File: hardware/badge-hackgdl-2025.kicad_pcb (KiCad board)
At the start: 2 copper layers, 73.4 x 79.5 mm, 53 parts, among them J1 ADDON, J2 Battery, P1 USB_C_Plug_USB2.0, Q1 DMG3415U-7, Q2 MMBT2222A, SW1 ON, SW2 RESET, SW3 BOOT, SW4 LEFT, SW5 BACK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

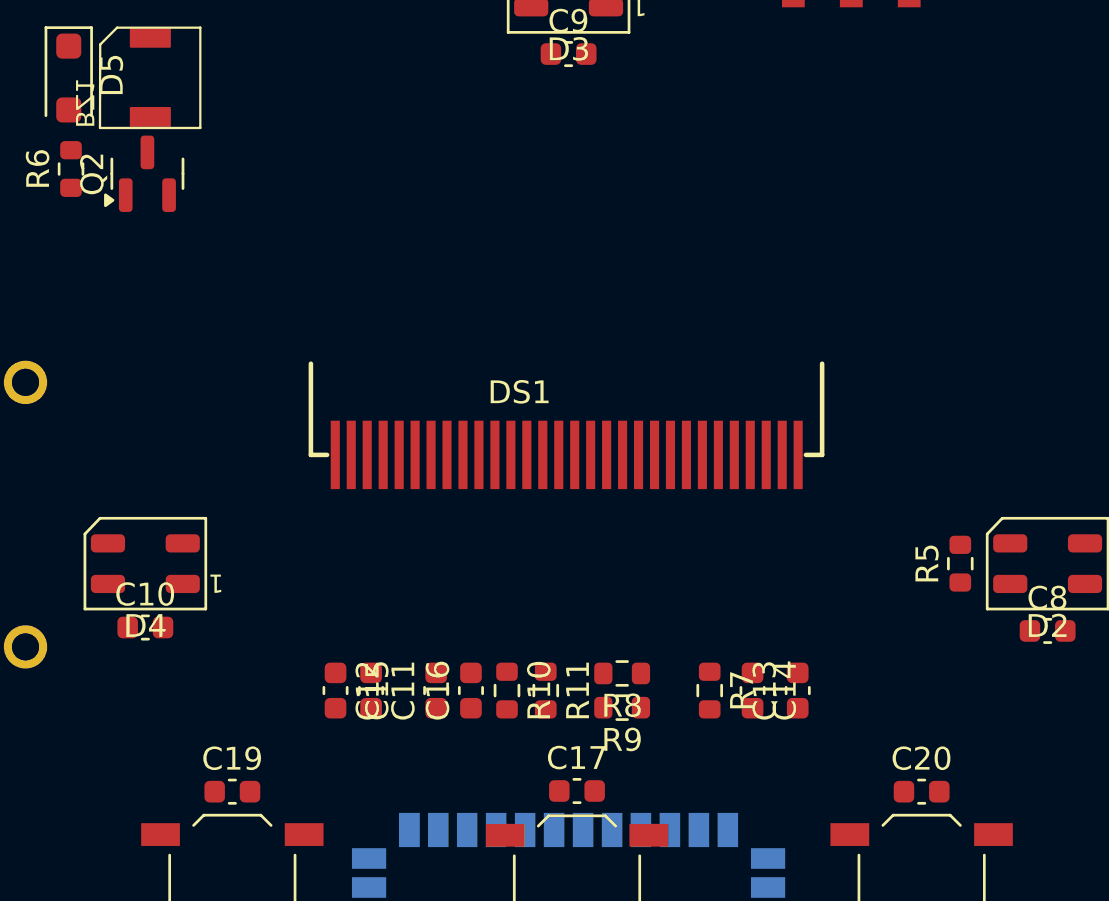
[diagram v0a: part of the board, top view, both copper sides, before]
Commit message: feat(hw): change oled footprint
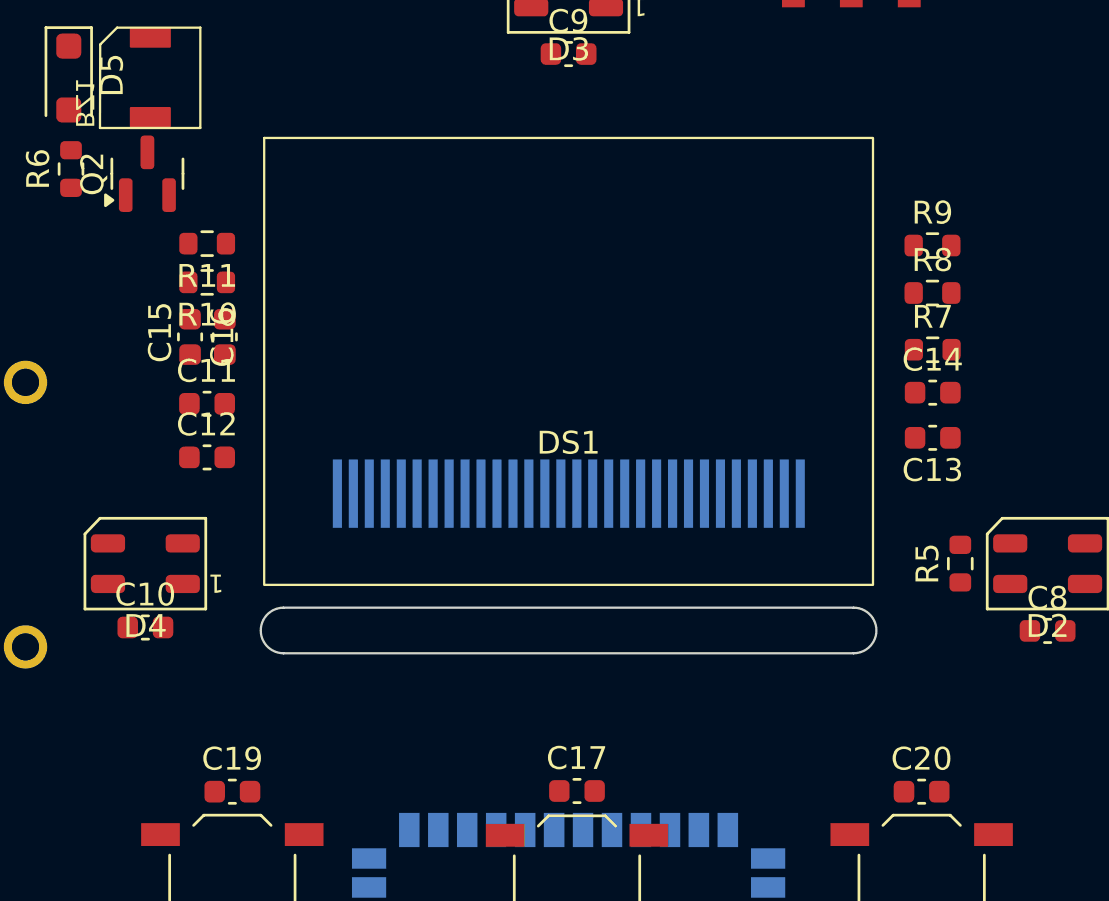
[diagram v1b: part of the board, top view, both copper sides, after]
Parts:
- DS1: footprint Footprints:ssd1306_oled_conn -> Footprints:ssd1306_oled_conn_through_the_oled
- R4: value 10K -> 10k
- moved R11 24.6 mm to (117.8, 47.7), turned to 180 degrees
- moved R9 24.4 mm to (149.6, 47.8), turned to 0 degrees
- moved R10 22.2 mm to (117.8, 49.4), turned to 180 degrees
- moved R8 21.5 mm to (149.6, 49.9), turned to 0 degrees
- moved C16 19.8 mm to (117.1, 51.8), turned to -90 degrees
- moved C15 18.1 mm to (118.6, 51.8), turned to -90 degrees
- moved R7 17.9 mm to (149.6, 52.3), turned to 0 degrees
- moved C14 15.3 mm to (149.6, 54.2), turned to 0 degrees
- moved C11 14.5 mm to (117.8, 54.7), turned to 0 degrees
- moved C13 12.6 mm to (149.6, 56.2), turned to 180 degrees
- moved C12 11.7 mm to (117.8, 57.1), turned to 0 degrees
- moved DS1 3.11 mm to (133.7, 56.9)
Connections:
- J1 pad 5: unconnected-(J1-Pin_5-Pad5) -> /GPIO1
- J1 pad 6: unconnected-(J1-Pin_6-Pad6) -> /GPIO2
- U2 pad 6: unconnected-(U2-IO6-Pad6) -> /GPIO1
- U2 pad 7: unconnected-(U2-IO7-Pad7) -> /GPIO2
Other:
- copper layers 2 -> 11

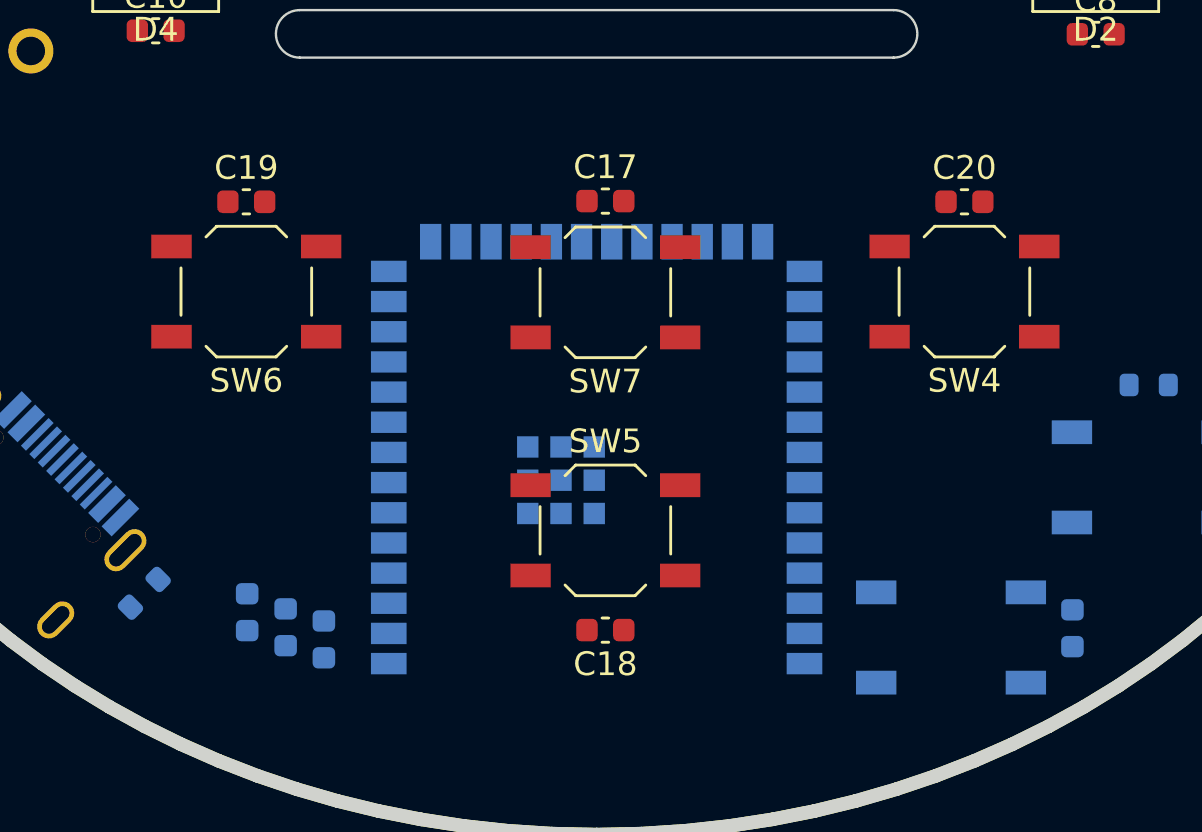
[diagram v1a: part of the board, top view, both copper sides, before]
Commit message: feat(hw): move buttons
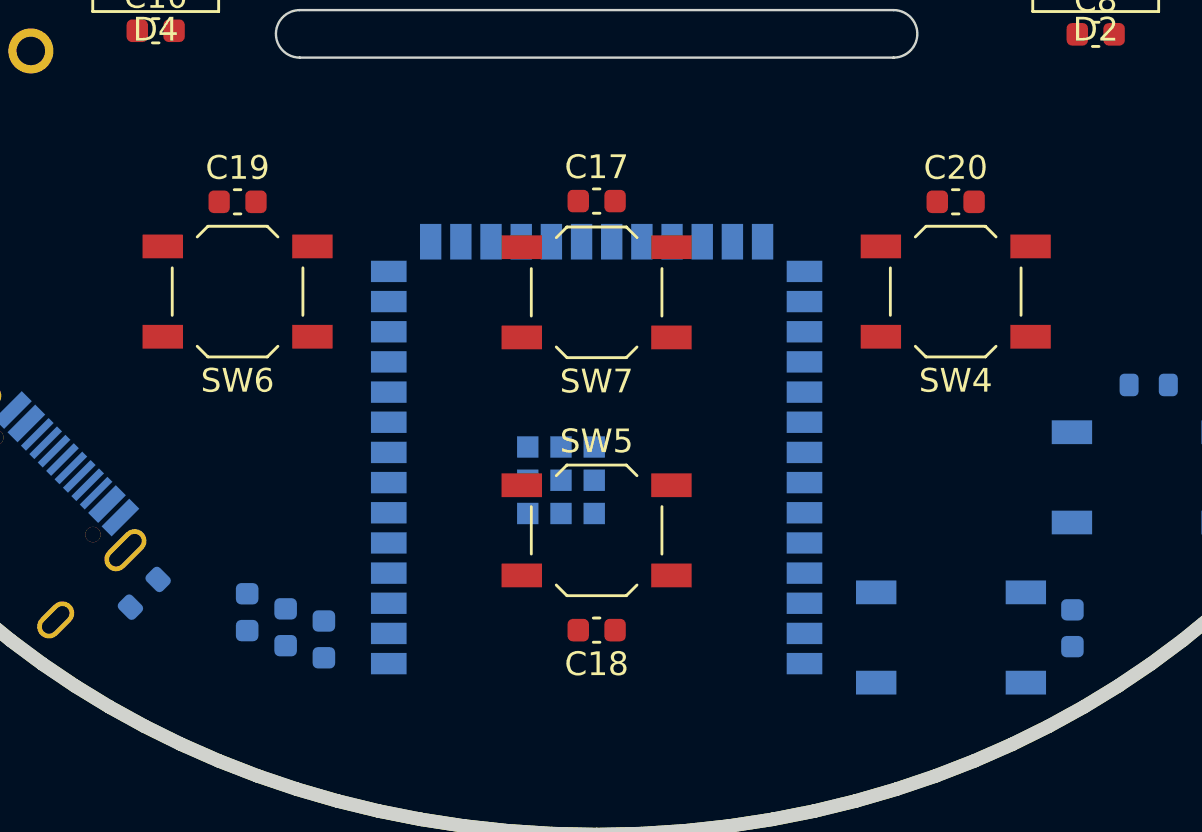
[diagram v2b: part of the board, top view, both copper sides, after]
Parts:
- moved C17 0.37 mm to (133.7, 71.7)
- moved C18 0.37 mm to (133.7, 89.8)
- moved C19 0.37 mm to (118.6, 71.7)
- moved C20 0.37 mm to (148.8, 71.7)
- moved SW4 0.37 mm to (148.8, 75.5)
- moved SW5 0.37 mm to (133.7, 85.5)
- moved SW6 0.37 mm to (118.6, 75.5)
- moved SW7 0.37 mm to (133.7, 75.5)
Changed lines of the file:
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@@
 		(0 "F.Cu" signal)
 		(2 "B.Cu" signal)
-		(9 "F.Adhes" user)
-		(11 "B.Adhes" user)
+		(9 "F.Adhes" user "F.Adhesive")
+		(11 "B.Adhes" user "B.Adhesive")
 		(13 "F.Paste" user)
 		(15 "B.Paste" user)
-		(5 "F.SilkS" user)
-		(7 "B.SilkS" user)
+		(5 "F.SilkS" user "F.Silkscreen")
+		(7 "B.SilkS" user "B.Silkscreen")
 		(1 "F.Mask" user)
 		(3 "B.Mask" user)
-		(17 "Dwgs.User" user)
-		(19 "Cmts.User" user)
-		(21 "Eco1.User" user)
-		(23 "Eco2.User" user)
+		(17 "Dwgs.User" user "User.Drawings")
+		(19 "Cmts.User" user "User.Comments")
+		(21 "Eco1.User" user "User.Eco1")
+		(23 "Eco2.User" user "User.Eco2")
 		(25 "Edge.Cuts" user)
 		(27 "Margin" user)
-		(31 "F.CrtYd" user)
-		(29 "B.CrtYd" user)
+		(31 "F.CrtYd" user "F.Courtyard")
+		(29 "B.CrtYd" user "B.Courtyard")
 		(35 "F.Fab" user)
 		(33 "B.Fab" user)
@@
 		(tags "resistor")
 		(property "Reference" "R8"
-			(at 0 -1.43 360)
+			(at 0 -1.43 0)
 			(layer "F.SilkS")
 			(effects
@@
 		)
 		(property "Value" "10k"
-			(at 0 1.43 360)
+			(at 0 1.43 0)
 			(layer "F.Fab")
 			(effects
@@
 		)
 		(property "Footprint" ""
-			(at 0 0 360)
+			(at 0 0 0)
 			(layer "F.Fab")
 			(hide yes)
@@
 		)
 		(fp_text user "${REFERENCE}"
-			(at 0 0 360)
+			(at 0 0 0)
 			(layer "F.Fab")
 			(effects
@@
 		)
 		(property "Footprint" ""
-			(at 0 0 90)
+			(at 0 0 -90)
 			(layer "F.Fab")
 			(hide yes)
@@
 		(tags "resistor")
 		(property "Reference" "R11"
-			(at 0 -1.43 360)
+			(at 0 -1.43 0)
 			(layer "F.SilkS")
 			(effects
@@
 		)
 		(property "Value" "10k"
-			(at 0 1.43 360)
+			(at 0 1.43 0)
 			(layer "F.Fab")
 			(effects
@@
 		)
 		(property "Footprint" ""
-			(at 0 0 360)
+			(at 0 0 180)
 			(layer "F.Fab")
 			(hide yes)
@@
 		)
 		(fp_text user "${REFERENCE}"
-			(at 0 0 360)
+			(at 0 0 0)
 			(layer "F.Fab")
 			(effects
@@
 		(tags "resistor")
 		(property "Reference" "R7"
-			(at 0 -1.43 360)
+			(at 0 -1.43 0)
 			(layer "F.SilkS")
 			(effects
@@
 		)
 		(property "Value" "390k"
-			(at 0 1.43 360)
+			(at 0 1.43 0)
 			(layer "F.Fab")
 			(effects
@@
 		)
 		(property "Footprint" ""
-			(at 0 0 360)
+			(at 0 0 0)
 			(layer "F.Fab")
 			(hide yes)
@@
 		)
 		(fp_text user "${REFERENCE}"
-			(at 0 0 360)
+			(at 0 0 0)
 			(layer "F.Fab")
 			(effects
@@
 		(tags "capacitor")
 		(property "Reference" "C11"
-			(at 0 -1.43 360)
+			(at 0 -1.43 0)
 			(layer "F.SilkS")
 			(effects
@@
 		)
 		(property "Value" "1uF"
-			(at 0 1.43 360)
+			(at 0 1.43 0)
 			(layer "F.Fab")
 			(effects
@@
 		)
 		(property "Footprint" ""
-			(at 0 0 360)
+			(at 0 0 0)
 			(layer "F.Fab")
 			(hide yes)
@@
 		)
 		(fp_text user "${REFERENCE}"
-			(at 0 0 360)
+			(at 0 0 0)
 			(layer "F.Fab")
 			(effects
@@
 		)
 		(property "Footprint" ""
-			(at 0 0 90)
+			(at 0 0 -90)
 			(layer "F.Fab")
 			(hide yes)
@@
 	(footprint "Button_Switch_SMD:SW_SPST_TL3342"
 		(layer "F.Cu")
-		(at 134.04 75.53 180)
+		(at 133.671189 75.53 180)
 		(descr "Low-profile SMD Tactile Switch, https://www.e-switch.com/system/asset/product_line/data_sheet/165/TL3342.pdf")
 		(tags "SPST Tactile Switch")
@@
 	(footprint "Button_Switch_SMD:SW_SPST_TL3342"
 		(layer "F.Cu")
-		(at 118.925 75.5 180)
+		(at 118.556189 75.5 180)
 		(descr "Low-profile SMD Tactile Switch, https://www.e-switch.com/system/asset/product_line/data_sheet/165/TL3342.pdf")
 		(tags "SPST Tactile Switch")
@@
 		(tags "capacitor")
 		(property "Reference" "C13"
-			(at 0 -1.43 360)
+			(at 0 -1.43 0)
 			(layer "F.SilkS")
 			(effects
@@
 		)
 		(property "Value" "10uF"
-			(at 0 1.43 360)
+			(at 0 1.43 0)
 			(layer "F.Fab")
 			(effects
@@
 		)
 		(property "Footprint" ""
-			(at 0 0 360)
+			(at 0 0 180)
 			(layer "F.Fab")
 			(hide yes)
@@
 		)
 		(fp_text user "${REFERENCE}"
-			(at 0 0 360)
+			(at 0 0 0)
 			(layer "F.Fab")
 			(effects
@@
 	(footprint "Capacitor_SMD:C_0603_1608Metric"
 		(layer "F.Cu")
-		(at 149.155 71.72)
+		(at 148.786189 71.72)
 		(descr "Capacitor SMD 0603 (1608 Metric), square (rectangular) end terminal, IPC_7351 nominal, (Body size source: IPC-SM-782 page 76, https://www.pcb-3d.com/wordpress/wp-content/uploads/ipc-sm-782a_amendment_1_and_2.pdf), generated with kicad-footprint-generator")
 		(tags "capacitor")
@@
 	(footprint "Capacitor_SMD:C_0603_1608Metric"
 		(layer "F.Cu")
-		(at 118.925 71.72)
+		(at 118.556189 71.72)
 		(descr "Capacitor SMD 0603 (1608 Metric), square (rectangular) end terminal, IPC_7351 nominal, (Body size source: IPC-SM-782 page 76, https://www.pcb-3d.com/wordpress/wp-content/uploads/ipc-sm-782a_amendment_1_and_2.pdf), generated with kicad-footprint-generator")
 		(tags "capacitor")
@@
 		(tags "capacitor")
 		(property "Reference" "C14"
-			(at 0 -1.43 360)
+			(at 0 -1.43 0)
 			(layer "F.SilkS")
 			(effects
@@
 		)
 		(property "Value" "10uF"
-			(at 0 1.43 360)
+			(at 0 1.43 0)
 			(layer "F.Fab")
 			(effects
@@
 		)
 		(property "Footprint" ""
-			(at 0 0 360)
+			(at 0 0 0)
 			(layer "F.Fab")
 			(hide yes)
@@
 		)
 		(fp_text user "${REFERENCE}"
-			(at 0 0 360)
+			(at 0 0 0)
 			(layer "F.Fab")
 			(effects
@@
 		(tags "capacitor")
 		(property "Reference" "C12"
-			(at 0 -1.43 360)
+			(at 0 -1.43 0)
 			(layer "F.SilkS")
 			(effects
@@
 		)
 		(property "Value" "1uF"
-			(at 0 1.43 360)
+			(at 0 1.43 0)
 			(layer "F.Fab")
 			(effects
@@
 		)
 		(property "Footprint" ""
-			(at 0 0 360)
+			(at 0 0 0)
 			(layer "F.Fab")
 			(hide yes)
@@
 		)
 		(fp_text user "${REFERENCE}"
-			(at 0 0 360)
+			(at 0 0 0)
 			(layer "F.Fab")
 			(effects
@@
 		(tags "resistor")
 		(property "Reference" "R10"
-			(at 0 -1.43 360)
+			(at 0 -1.43 0)
 			(layer "F.SilkS")
 			(effects
@@
 		)
 		(property "Value" "10k"
-			(at 0 1.43 360)
+			(at 0 1.43 0)
 			(layer "F.Fab")
 			(effects
@@
 		)
 		(property "Footprint" ""
-			(at 0 0 360)
+			(at 0 0 180)
 			(layer "F.Fab")
 			(hide yes)
@@
 		)
 		(fp_text user "${REFERENCE}"
-			(at 0 0 360)
+			(at 0 0 0)
 			(layer "F.Fab")
 			(effects
@@
 	(footprint "Button_Switch_SMD:SW_SPST_TL3342"
 		(layer "F.Cu")
-		(at 134.04 85.55)
+		(at 133.671189 85.55)
 		(descr "Low-profile SMD Tactile Switch, https://www.e-switch.com/system/asset/product_line/data_sheet/165/TL3342.pdf")
 		(tags "SPST Tactile Switch")
@@
 	(footprint "Capacitor_SMD:C_0603_1608Metric"
 		(layer "F.Cu")
-		(at 134.04 89.75 180)
+		(at 133.671189 89.75 180)
 		(descr "Capacitor SMD 0603 (1608 Metric), square (rectangular) end terminal, IPC_7351 nominal, (Body size source: IPC-SM-782 page 76, https://www.pcb-3d.com/wordpress/wp-content/uploads/ipc-sm-782a_amendment_1_and_2.pdf), generated with kicad-footprint-generator")
 		(tags "capacitor")
@@
 		(tags "resistor")
 		(property "Reference" "R9"
-			(at 0 -1.43 360)
+			(at 0 -1.43 0)
 			(layer "F.SilkS")
 			(effects
@@
 		)
 		(property "Value" "10k"
-			(at 0 1.43 360)
+			(at 0 1.43 0)
 			(layer "F.Fab")
 			(effects
@@
 		)
 		(property "Footprint" ""
-			(at 0 0 360)
+			(at 0 0 0)
 			(layer "F.Fab")
 			(hide yes)
@@
 		)
 		(fp_text user "${REFERENCE}"
-			(at 0 0 360)
+			(at 0 0 0)
 			(layer "F.Fab")
 			(effects
@@
 	(footprint "Button_Switch_SMD:SW_SPST_TL3342"
 		(layer "F.Cu")
-		(at 149.155 75.5 180)
+		(at 148.786189 75.5 180)
 		(descr "Low-profile SMD Tactile Switch, https://www.e-switch.com/system/asset/product_line/data_sheet/165/TL3342.pdf")
 		(tags "SPST Tactile Switch")
@@
 	(footprint "Capacitor_SMD:C_0603_1608Metric"
 		(layer "F.Cu")
-		(at 134.04 71.69)
+		(at 133.671189 71.69)
 		(descr "Capacitor SMD 0603 (1608 Metric), square (rectangular) end terminal, IPC_7351 nominal, (Body size source: IPC-SM-782 page 76, https://www.pcb-3d.com/wordpress/wp-content/uploads/ipc-sm-782a_amendment_1_and_2.pdf), generated with kicad-footprint-generator")
 		(tags "capacitor")
